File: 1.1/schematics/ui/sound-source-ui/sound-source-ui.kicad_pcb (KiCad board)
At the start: 2 copper layers, 120 x 100 mm, 14 parts

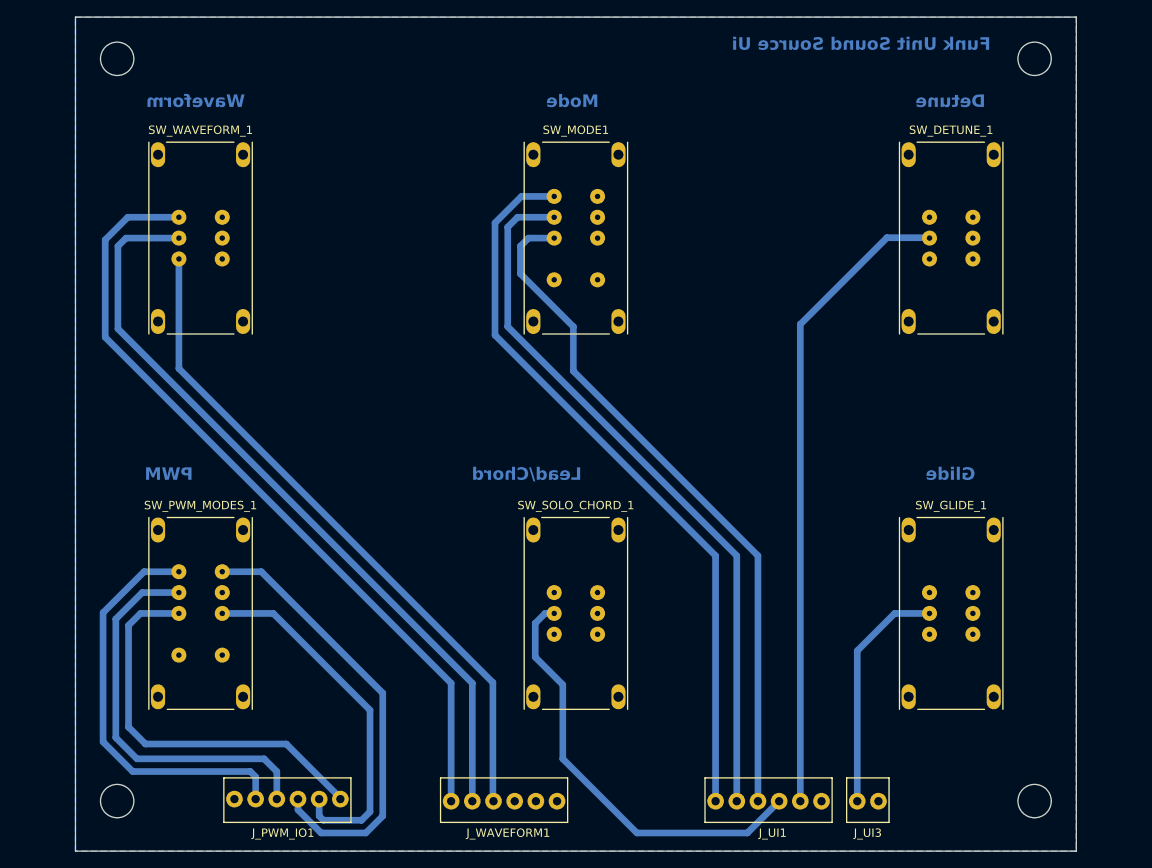
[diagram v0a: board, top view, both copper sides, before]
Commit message: Added envelope UI connections
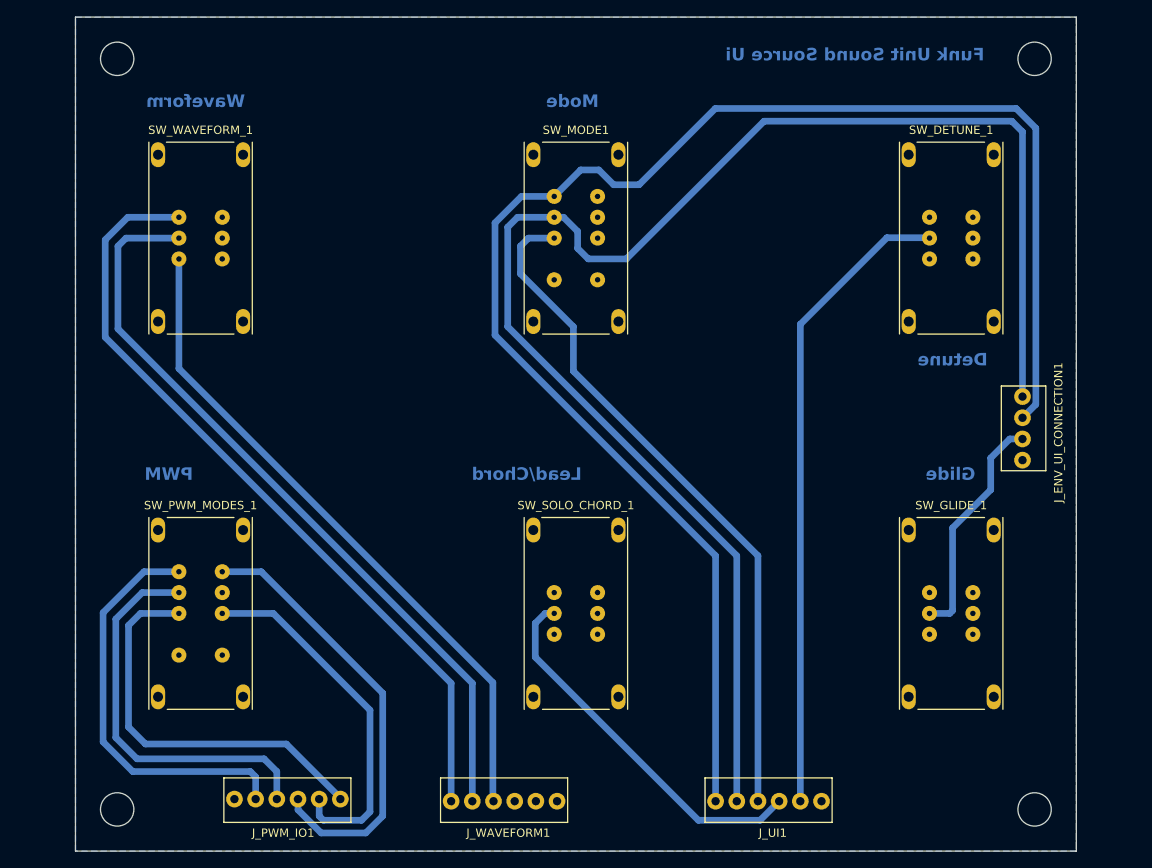
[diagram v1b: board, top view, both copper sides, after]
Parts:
- removed J_UI3: Conn_01x02, Shmoergh_Custom_Footprints:NSL25_01x02_Vertical
- added J_ENV_UI_CONNECTION1: Conn_01x04, Shmoergh_Custom_Footprints:NSL25_01x04_Vertical, F.Cu at (193.5, 79.5)
- moved H3 1.00 mm to (195.0, 129.0)
- moved H4 1.00 mm to (85.0, 129.0)
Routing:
- net +3.3V: track 88.7 -> 188.7 mm
- net 1.5V: track 86.3 -> 184.8 mm
- net SOLO_CHORD: track 51.6 -> 45.1 mm
- net GLIDE: track 28.6 -> 27.8 mm

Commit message: Made sound source UI PCB narrower
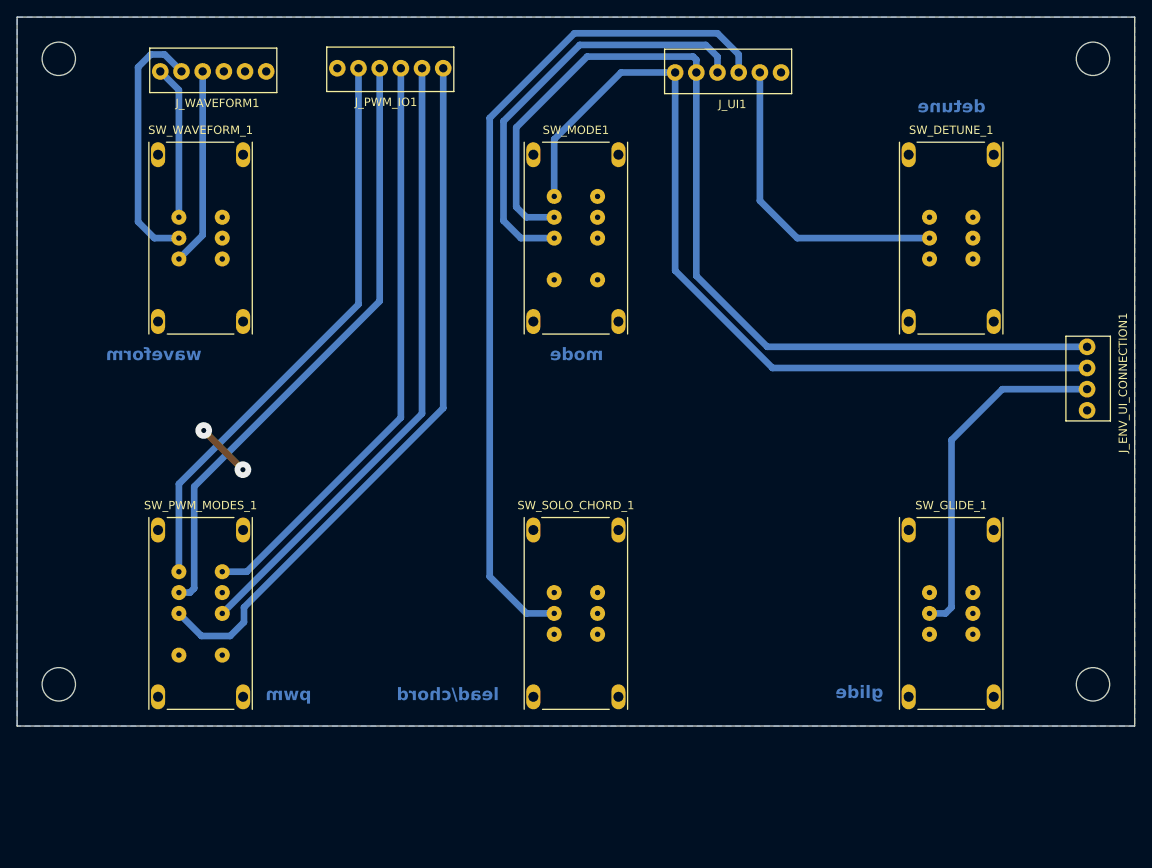
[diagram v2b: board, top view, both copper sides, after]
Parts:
- moved J_WAVEFORM1 94.2 mm to (90.2, 40.5)
- moved J_PWM_IO1 88.5 mm to (124.1, 40.1)
- moved J_UI1 87.5 mm to (151.9, 40.6)
- moved H3 16.6 mm to (202.0, 114.0)
- moved H4 16.6 mm to (78.0, 114.0)
- moved J_ENV_UI_CONNECTION1 9.78 mm to (201.3, 73.5)
- moved H1 7.00 mm to (78.0, 39.0)
- moved H2 7.00 mm to (202.0, 39.0)
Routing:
- net +3.3V: track 188.7 -> 102.7 mm
- net SQR_IN: track 94.4 -> 18.4 mm
- net 1.5V: track 184.8 -> 116.2 mm
- net WAVEFORM_OUT: track 91.9 -> 30.9 mm
- net SAW_IN: track 80.6 -> 23.7 mm
- net SOLO_CHORD: track 45.1 -> 101.8 mm
- net DETUNE: track 77.0 -> 37.6 mm
- net PULSE_WIDTH: track 47.9 -> 85.9 mm
- net MODE: track 82.8 -> 50.8 mm
- net PWM_OUT: track 43.5 -> 75.3 mm
- net PWM_NARROW_BIAS: track 47.4 -> 73.6 mm
- net PWM_LFO_BIAS: track 49.3 -> 69.3 mm
- net PWM_LFO: track 53.4 -> 71.0 mm
- net GLIDE: track 27.8 -> 41.8 mm
- net GND: track 0.00 -> 6.65 mm, vias 0 -> 2
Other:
- board size 120 x 100 mm -> 134 x 85 mm
- board text added: "detune"
- board text added: "glide"
- board text added: "lead/chord"
- board text added: "mode"
- board text added: "pwm"
- board text added: "waveform"
- board text removed: "Detune"
- board text removed: "Funk Unit Sound Source Ui"
- board text removed: "Glide"
- board text removed: "Lead/Chord"
- board text removed: "Mode"
- board text removed: "PWM"
- board text removed: "Waveform"

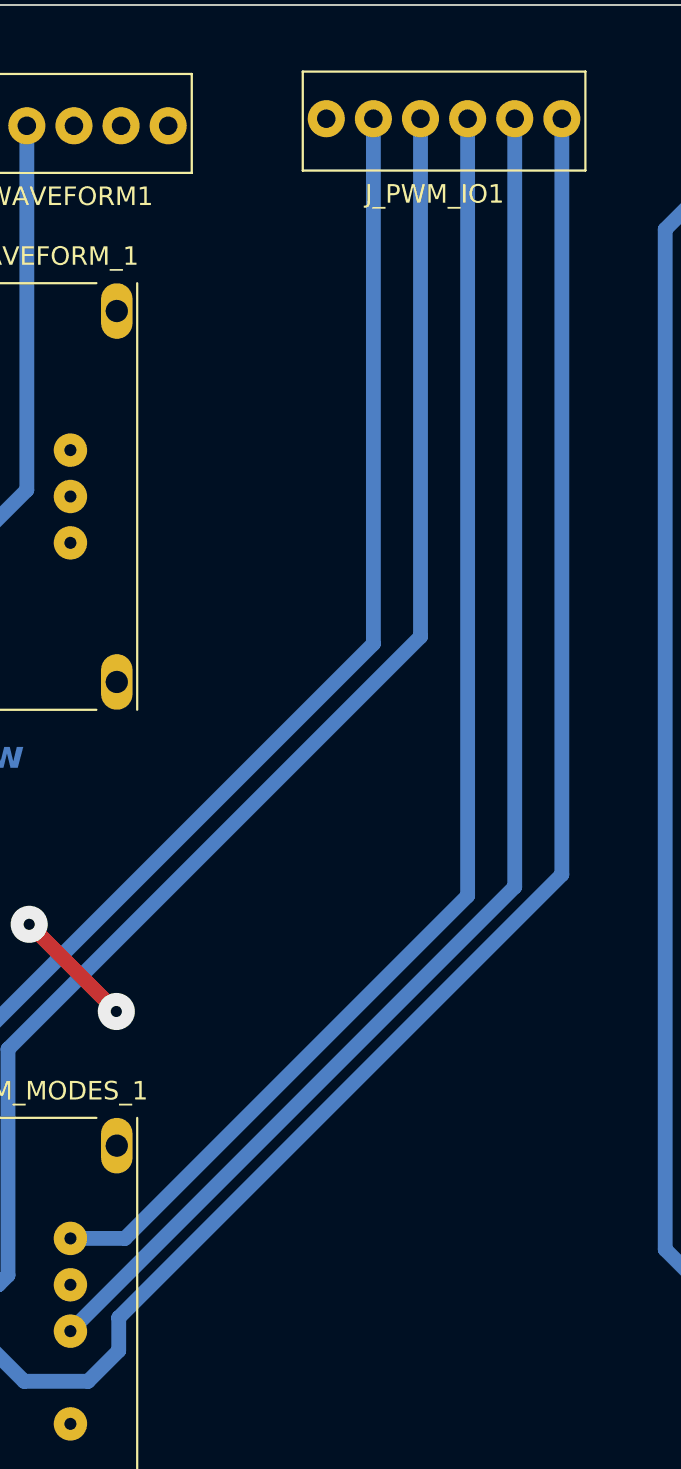
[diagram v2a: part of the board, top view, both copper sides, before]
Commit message: Updated envelope UI and filter
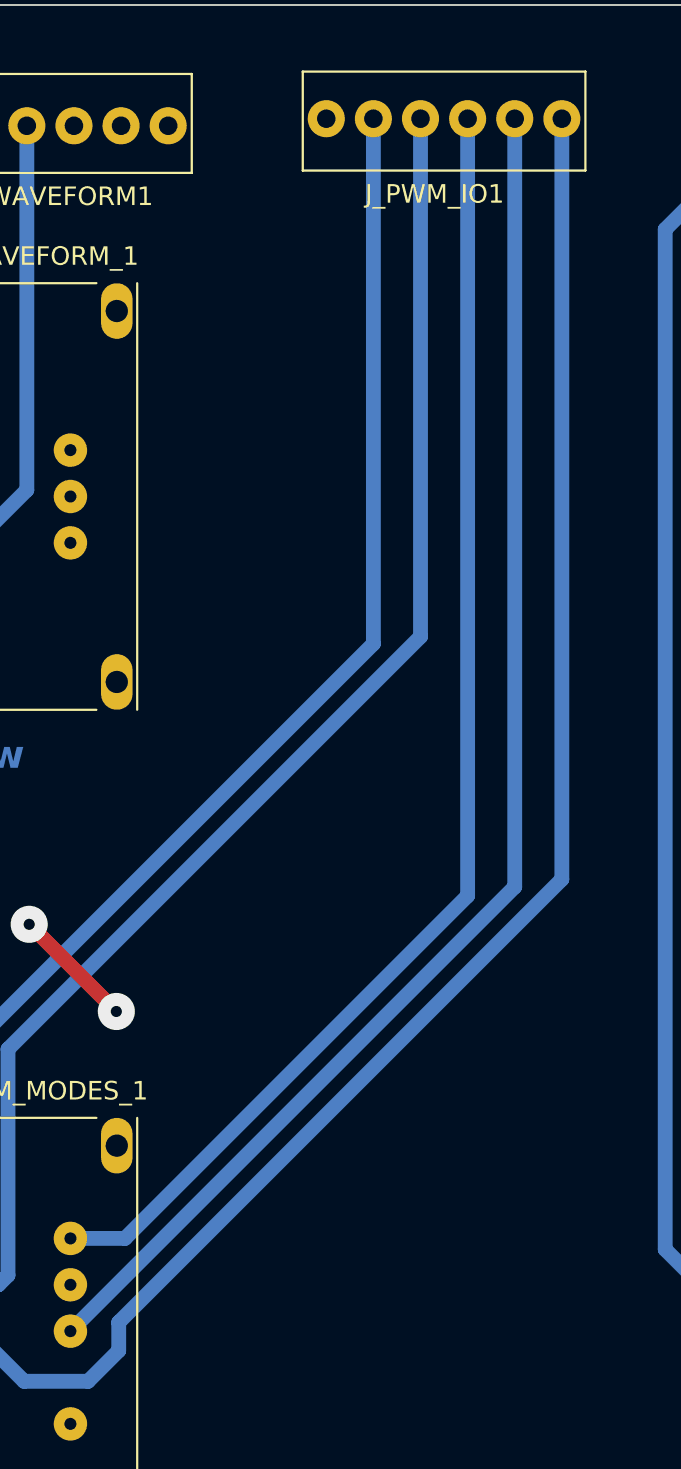
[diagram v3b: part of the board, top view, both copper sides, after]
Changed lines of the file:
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@@
     (pad_to_mask_clearance 0)
     (pcbplotparams
-      (layerselection 0x00010fc_ffffffff)
+      (layerselection 0x0000000_fffffffe)
       (plot_on_all_layers_selection 0x0000000_00000000)
       (disableapertmacros false)
@@
       (sketchpadsonfab false)
       (subtractmaskfromsilk false)
-      (outputformat 1)
+      (outputformat 4)
       (mirror false)
-      (drillshape 1)
+      (drillshape 2)
       (scaleselection 1)
-      (outputdirectory "")
+      (outputdirectory "plot/")
     )
   )
@@
     (style (thickness 0.15) (arrow_length 1.27) (text_position_mode 0) (extension_height 0.58642) (extension_offset 0.5) keep_text_aligned)
   )
+  (segment (start 100.203 105.029) (end 100.203 106.553) (width 0.8) (layer "B.Cu") (net 1))
+  (segment (start 98.552 108.204) (end 95.104 108.204) (width 0.8) (layer "B.Cu") (net 1))
+  (segment (start 124.094314 81.137686) (end 100.203 105.029) (width 0.8) (layer "B.Cu") (net 1))
+  (segment (start 100.203 106.553) (end 98.552 108.204) (width 0.8) (layer "B.Cu") (net 1))
+  (segment (start 124.094314 40.132) (end 124.094314 81.137686) (width 0.8) (layer "B.Cu") (net 1))
   (segment (start 95.104 108.204) (end 92.4 105.5) (width 0.8) (layer "B.Cu") (net 1))
-  (segment (start 98.552 108.204) (end 95.104 108.204) (width 0.8) (layer "B.Cu") (net 1))
-  (segment (start 100.203 106.553) (end 98.552 108.204) (width 0.8) (layer "B.Cu") (net 1))
-  (segment (start 124.094314 40.132) (end 124.094314 80.883686) (width 0.8) (layer "B.Cu") (net 1))
-  (segment (start 100.203 104.775) (end 100.203 106.553) (width 0.8) (layer "B.Cu") (net 1))
-  (segment (start 124.094314 80.883686) (end 100.203 104.775) (width 0.8) (layer "B.Cu") (net 1))
   (segment (start 121.554314 81.545686) (end 97.6 105.5) (width 0.8) (layer "B.Cu") (net 2))
   (segment (start 121.554314 40.132) (end 121.554314 81.545686) (width 0.8) (layer "B.Cu") (net 2))
